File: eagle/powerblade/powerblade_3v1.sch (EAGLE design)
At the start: 79 parts, among them J1 JTAG_14PIN_IDC-NL, J21 AC_INSLOT2, J4 TC2030-JLINK-NL, Q1 2N7002, Q4 2SK1829, U1 TPS62122, U2 MCP6V3, U3 MSP430FR5738, U4 NRF51822QF, U6 MAX9910, U7 OPA2369, X1 16MHz, X3 32.768kHz, Y1 UREACH_XTEND

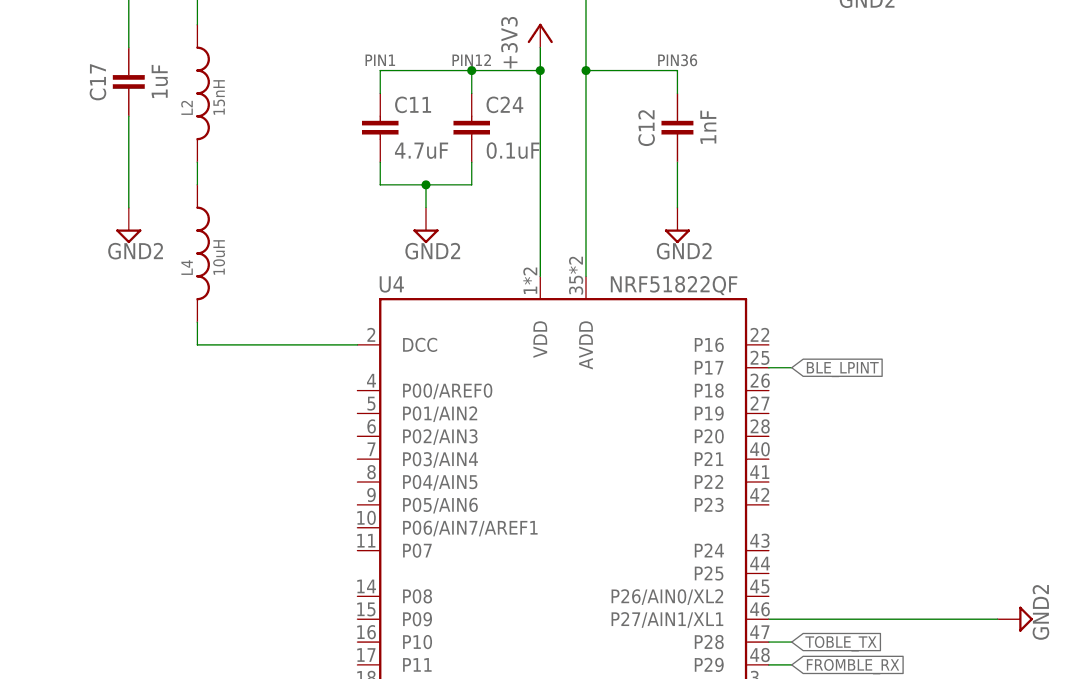
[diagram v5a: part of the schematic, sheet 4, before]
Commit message: finished routing supply in backwards
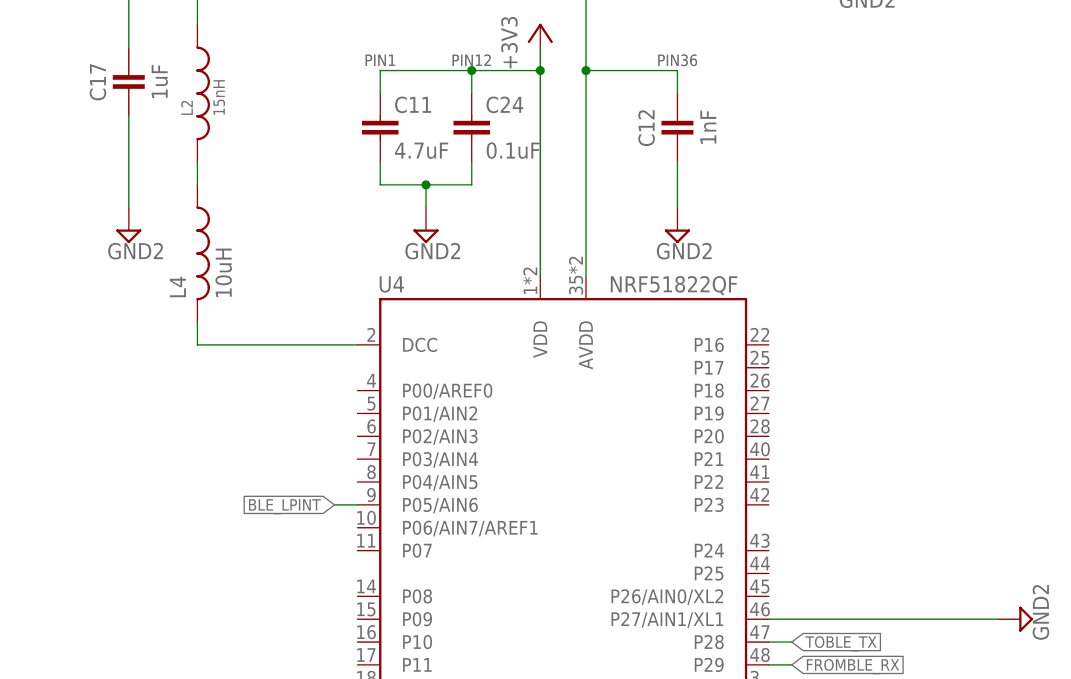
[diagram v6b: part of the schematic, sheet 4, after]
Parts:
- C5: device rcl:C-EUC0805_SM -> rcl:C-EUC0603_TN; DIGIKEY 445-9077-1-ND -> (none)
- C7: device rcl:C-EUC0603_SM -> rcl:C-EUC0402_SM
- L4: device passives:INDUCTOR0603 -> rcl:L-USL0603_TN
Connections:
- net BLE_LPINT: now also U4.P05/AIN6; no longer U4.P17

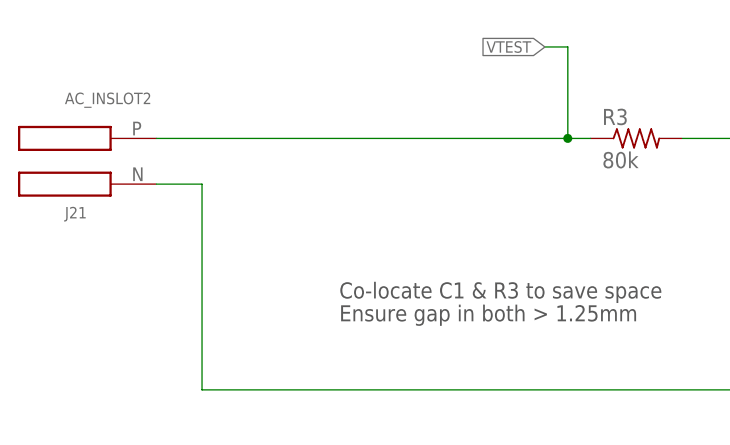
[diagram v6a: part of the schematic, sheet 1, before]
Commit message: down to 9 airwires
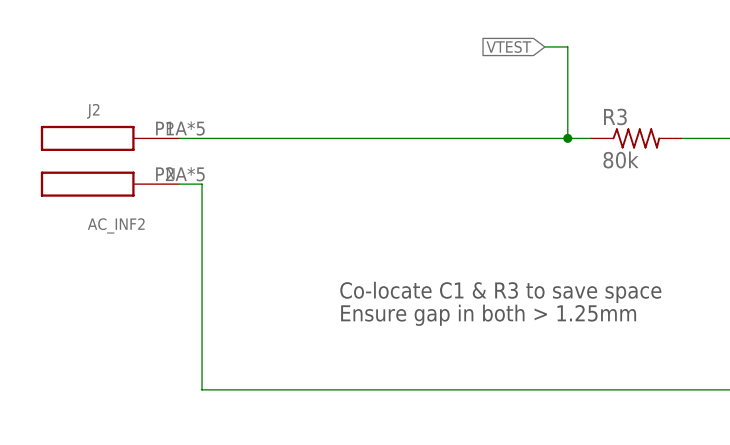
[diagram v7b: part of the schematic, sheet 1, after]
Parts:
- removed J21: AC_INSLOT2, powerfilm:AC_INSLOT2
- added J2: AC_INF2, powerfilm:AC_INF2
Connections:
- net TDO renamed N$2
- net +3V3: now also SV1.8; no longer SV1.9
- net BLE_ENABLE: now also U3.P1.6/TA0.0/UCBSDA/MOSI; no longer U3.P2.2/UCBCLK
- net BLE_LPINT: now also U3.P1.7/TA1.0/UCBSCL/MISO; no longer U3.P1.6/TA0.0/UCBSDA/MOSI
- net GND: now also J2.N, SV1.7; no longer J21.P, SV1.11
- net I_SENSE: now also SV1.6, U3.P1.0/VREF-; no longer SV1.3, U3.P1.5/TB0.2/UCACLK
- net METER_ENABLE: now also U3.P2.2/UCBCLK; no longer U3.P1.7/TA1.0/UCBSCL/MISO
- net PWM_VOLTAGE: now also SV1.4; no longer SV1.6
- net VAMP: now also SV1.9; no longer SV1.7
- net VCC_SENSE: now also U3.P1.5/TB0.2/UCACLK; no longer U3.P1.1/VREF+
- net VTEST: now also J2.P; no longer J21.N
- net V_SENSE: now also SV1.3; no longer SV1.4
- net ZC: now also SV1.11; no longer SV1.8
- net ZC_LOW: now also U3.P1.1/VREF+; no longer U3.P1.0/VREF-
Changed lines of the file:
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@@
 <part name="GND1" library="supply1" deviceset="GND" device=""/>
 <part name="P+1" library="supply1" deviceset="VCC" device=""/>
-<part name="J21" library="powerfilm" deviceset="AC_IN" device="SLOT2" value="AC_INSLOT2">
-<attribute name="DIGIKEY" value="NP"/>
-</part>
 <part name="U1" library="powerfilm" deviceset="TPS62122" device=""/>
 <part name="L1" library="rcl" deviceset="L-US" device="L0805" value="10uH">
@@
 <attribute name="DIGIKEY" value="490-4025-1-ND"/>
 </part>
+<part name="J2" library="powerfilm" deviceset="AC_IN" device="F2"/>
 </parts>
 <sheets>
@@
 <instance part="GND1" gate="1" x="93.98" y="-22.86"/>
 <instance part="P+1" gate="VCC" x="93.98" y="27.94"/>
-<instance part="J21" gate="G$1" x="-45.72" y="15.24" rot="MR180">
-<attribute name="DIGIKEY" x="-45.72" y="15.24" size="1.27" layer="96" rot="MR180" display="off"/>
-</instance>
 <instance part="R3" gate="G$1" x="15.24" y="17.78">
 <attribute name="DIGIKEY" x="15.24" y="17.78" size="1.27" layer="96" display="off"/>
@@
 <attribute name="DIGIKEY" x="104.14" y="5.08" size="1.27" layer="96" display="off"/>
 </instance>
+<instance part="J2" gate="G$1" x="-43.18" y="15.24"/>
 </instances>
 <busses>
@@
 <pinref part="R3" gate="G$1" pin="1"/>
 <wire x1="7.62" y1="17.78" x2="10.16" y2="17.78" width="0.1524" layer="91"/>
-<pinref part="J21" gate="G$1" pin="N"/>
-<wire x1="-38.1" y1="17.78" x2="7.62" y2="17.78" width="0.1524" layer="91"/>
 <junction x="7.62" y="17.78"/>
+<pinref part="J2" gate="G$1" pin="P"/>
+<wire x1="-35.56" y1="17.78" x2="7.62" y2="17.78" width="0.1524" layer="91"/>
 </segment>
 </net>
@@
 <pinref part="C1" gate="G$1" pin="-"/>
 <wire x1="104.14" y1="0" x2="104.14" y2="-10.16" width="0.1524" layer="91"/>
-<pinref part="J21" gate="G$1" pin="P"/>
-<wire x1="-38.1" y1="12.7" x2="-33.02" y2="12.7" width="0.1524" layer="91"/>
+<pinref part="J2" gate="G$1" pin="N"/>
+<wire x1="-35.56" y1="12.7" x2="-33.02" y2="12.7" width="0.1524" layer="91"/>
 </segment>
 </net>
@@
 </segment>
 </net>
-<net name="TDO" class="0">
+<net name="N$2" class="0">
 <segment>
 <pinref part="U3" gate="G$1" pin="TDO"/>
@@
 <net name="BLE_ENABLE" class="0">
 <segment>
-<pinref part="U3" gate="G$1" pin="P2.2/UCBCLK"/>
-<wire x1="27.94" y1="-10.16" x2="25.4" y2="-10.16" width="0.1524" layer="91"/>
-<label x="27.94" y="-10.16" size="1.27" layer="95" xref="yes"/>
+<wire x1="27.94" y1="2.54" x2="25.4" y2="2.54" width="0.1524" layer="91"/>
+<label x="27.94" y="2.54" size="1.27" layer="95" xref="yes"/>
+<pinref part="U3" gate="G$1" pin="P1.6/TA0.0/UCBSDA/MOSI"/>
 </segment>
 </net>
@@
 <net name="I_SENSE" class="0">
 <segment>
-<pinref part="U3" gate="G$1" pin="P1.5/TB0.2/UCACLK"/>
-<wire x1="27.94" y1="5.08" x2="25.4" y2="5.08" width="0.1524" layer="91"/>
-<label x="27.94" y="5.08" size="1.27" layer="95" xref="yes"/>
+<label x="27.94" y="17.78" size="1.27" layer="95" xref="yes"/>
+<pinref part="U3" gate="G$1" pin="P1.0/VREF-"/>
+<wire x1="25.4" y1="17.78" x2="27.94" y2="17.78" width="0.1524" layer="91"/>
 </segment>
 </net>
 <net name="METER_ENABLE" class="0">
 <segment>
-<pinref part="U3" gate="G$1" pin="P1.7/TA1.0/UCBSCL/MISO"/>
-<wire x1="27.94" y1="0" x2="25.4" y2="0" width="0.1524" layer="91"/>
-<label x="27.94" y="0" size="1.27" layer="95" xref="yes"/>
+<label x="27.94" y="-10.16" size="1.27" layer="95" xref="yes"/>
+<pinref part="U3" gate="G$1" pin="P2.2/UCBCLK"/>
+<wire x1="25.4" y1="-10.16" x2="27.94" y2="-10.16" width="0.1524" layer="91"/>
 </segment>
 </net>
@@
 </segment>
 <segment>
-<label x="27.94" y="15.24" size="1.27" layer="95" xref="yes"/>
-<pinref part="U3" gate="G$1" pin="P1.1/VREF+"/>
-<wire x1="25.4" y1="15.24" x2="27.94" y2="15.24" width="0.1524" layer="91"/>
+<label x="27.94" y="5.08" size="1.27" layer="95" xref="yes"/>
+<wire x1="25.4" y1="5.08" x2="27.94" y2="5.08" width="0.1524" layer="91"/>
+<pinref part="U3" gate="G$1" pin="P1.5/TB0.2/UCACLK"/>
 </segment>
 </net>
@@
 <net name="BLE_LPINT" class="0">
 <segment>
-<pinref part="U3" gate="G$1" pin="P1.6/TA0.0/UCBSDA/MOSI"/>
-<wire x1="27.94" y1="2.54" x2="25.4" y2="2.54" width="0.1524" layer="91"/>
-<label x="27.94" y="2.54" size="1.27" layer="95" xref="yes"/>
+<label x="27.94" y="0" size="1.27" layer="95" xref="yes"/>
+<wire x1="27.94" y1="0" x2="25.4" y2="0" width="0.1524" layer="91"/>
+<pinref part="U3" gate="G$1" pin="P1.7/TA1.0/UCBSCL/MISO"/>
 </segment>
 </net>
@@
 <wire x1="60.96" y1="10.16" x2="60.96" y2="7.62" width="0.1524" layer="91"/>
 <junction x="60.96" y="10.16"/>
-<pinref part="U3" gate="G$1" pin="P1.0/VREF-"/>
-<wire x1="25.4" y1="17.78" x2="50.8" y2="17.78" width="0.1524" layer="91"/>
-<wire x1="50.8" y1="17.78" x2="50.8" y2="10.16" width="0.1524" layer="91"/>
-<label x="27.94" y="17.78" size="1.524" layer="95"/>
+<label x="45.72" y="15.24" size="1.524" layer="95"/>
+<pinref part="U3" gate="G$1" pin="P1.1/VREF+"/>
+<wire x1="25.4" y1="15.24" x2="50.8" y2="15.24" width="0.1524" layer="91"/>
+<wire x1="50.8" y1="15.24" x2="50.8" y2="10.16" width="0.1524" layer="91"/>
 </segment>
 </net>
@@
 <attribute name="DIGIKEY" x="0" y="0" size="1.27" layer="96" display="off"/>
 </instance>
-<instance part="GND9" gate="1" x="40.64" y="7.62"/>
+<instance part="GND9" gate="1" x="40.64" y="-5.08"/>
 <instance part="+3V2" gate="G$1" x="30.48" y="22.86"/>
 <instance part="P+3" gate="VCC" x="22.86" y="22.86"/>
@@
 <net name="PWM_VOLTAGE" class="0">
 <segment>
-<pinref part="SV1" gate="1" pin="6"/>
+<label x="10.16" y="-5.08" size="1.27" layer="95" xref="yes"/>
+<pinref part="SV1" gate="1" pin="4"/>
+<wire x1="7.62" y1="-5.08" x2="10.16" y2="-5.08" width="0.1524" layer="91"/>
+</segment>
+</net>
+<net name="V_SENSE" class="0">
+<segment>
+<label x="10.16" y="-7.62" size="1.27" layer="95" xref="yes"/>
+<pinref part="SV1" gate="1" pin="3"/>
+<wire x1="7.62" y1="-7.62" x2="10.16" y2="-7.62" width="0.1524" layer="91"/>
+</segment>
+</net>
+<net name="I_SENSE" class="0">
+<segment>
 <wire x1="10.16" y1="0" x2="7.62" y2="0" width="0.1524" layer="91"/>
 <label x="10.16" y="0" size="1.27" layer="95" xref="yes"/>
-</segment>
-</net>
-<net name="V_SENSE" class="0">
-<segment>
-<pinref part="SV1" gate="1" pin="4"/>
-<wire x1="10.16" y1="-5.08" x2="7.62" y2="-5.08" width="0.1524" layer="91"/>
-<label x="10.16" y="-5.08" size="1.27" layer="95" xref="yes"/>
-</segment>
-</net>
-<net name="I_SENSE" class="0">
-<segment>
-<pinref part="SV1" gate="1" pin="3"/>
-<wire x1="10.16" y1="-7.62" x2="7.62" y2="-7.62" width="0.1524" layer="91"/>
-<label x="10.16" y="-7.62" size="1.27" layer="95" xref="yes"/>
+<pinref part="SV1" gate="1" pin="6"/>
 </segment>
 </net>
@@
 <segment>
 <pinref part="GND9" gate="1" pin="GND"/>
-<pinref part="SV1" gate="1" pin="11"/>
-<wire x1="40.64" y1="12.7" x2="40.64" y2="10.16" width="0.1524" layer="91"/>
-<wire x1="7.62" y1="12.7" x2="40.64" y2="12.7" width="0.1524" layer="91"/>
+<wire x1="40.64" y1="2.54" x2="40.64" y2="-2.54" width="0.1524" layer="91"/>
+<pinref part="SV1" gate="1" pin="7"/>
+<wire x1="7.62" y1="2.54" x2="40.64" y2="2.54" width="0.1524" layer="91"/>
 </segment>
 </net>
@@
 <segment>
 <pinref part="+3V2" gate="G$1" pin="+3V3"/>
-<wire x1="30.48" y1="7.62" x2="30.48" y2="20.32" width="0.1524" layer="91"/>
-<pinref part="SV1" gate="1" pin="9"/>
-<wire x1="7.62" y1="7.62" x2="30.48" y2="7.62" width="0.1524" layer="91"/>
+<wire x1="30.48" y1="5.08" x2="30.48" y2="20.32" width="0.1524" layer="91"/>
+<pinref part="SV1" gate="1" pin="8"/>
+<wire x1="7.62" y1="5.08" x2="30.48" y2="5.08" width="0.1524" layer="91"/>
 </segment>
 </net>
@@
 <net name="ZC" class="0">
 <segment>
-<pinref part="SV1" gate="1" pin="8"/>
-<wire x1="10.16" y1="5.08" x2="7.62" y2="5.08" width="0.1524" layer="91"/>
-<label x="10.16" y="5.08" size="1.27" layer="95" xref="yes"/>
+<wire x1="10.16" y1="12.7" x2="7.62" y2="12.7" width="0.1524" layer="91"/>
+<label x="10.16" y="12.7" size="1.27" layer="95" xref="yes"/>
+<pinref part="SV1" gate="1" pin="11"/>
 </segment>
 </net>
 <net name="VAMP" class="0">
 <segment>
-<pinref part="SV1" gate="1" pin="7"/>
-<wire x1="10.16" y1="2.54" x2="7.62" y2="2.54" width="0.1524" layer="91"/>
-<label x="10.16" y="2.54" size="1.27" layer="95" xref="yes"/>
-</segment>
-</net>
+<wire x1="10.16" y1="7.62" x2="7.62" y2="7.62" width="0.1524" layer="91"/>
+<label x="10.16" y="7.62" size="1.27" layer="95" xref="yes"/>
+<pinref part="SV1" gate="1" pin="9"/>
+</segment>
+</net>
